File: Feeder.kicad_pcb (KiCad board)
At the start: 6 copper layers, 32 x 40 mm, 51 parts, among them T502 CMB1670V, U702 TPS562202, U710 TPS562202

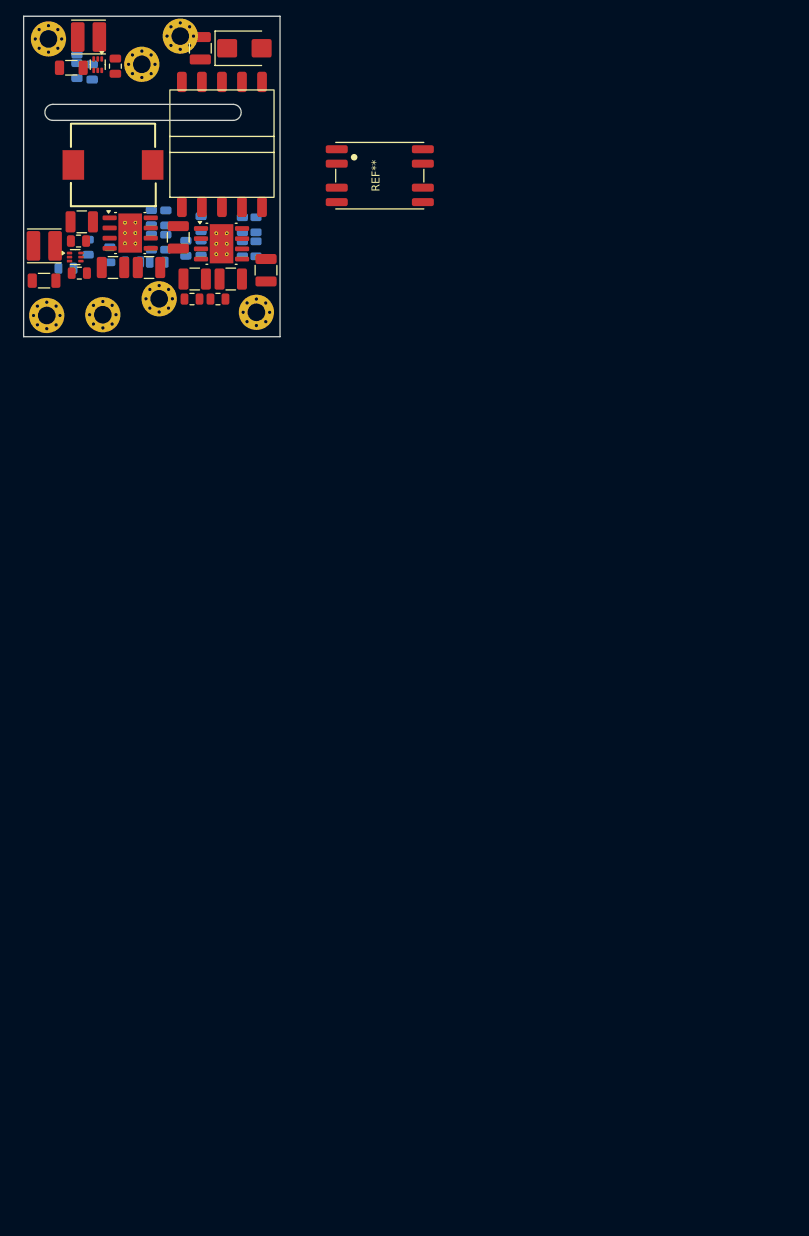
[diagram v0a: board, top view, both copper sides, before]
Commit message: Adding the placeholder for the capacitor board.
Signed-off-by: Jean Alinei <jean.alinei@owntech.org>
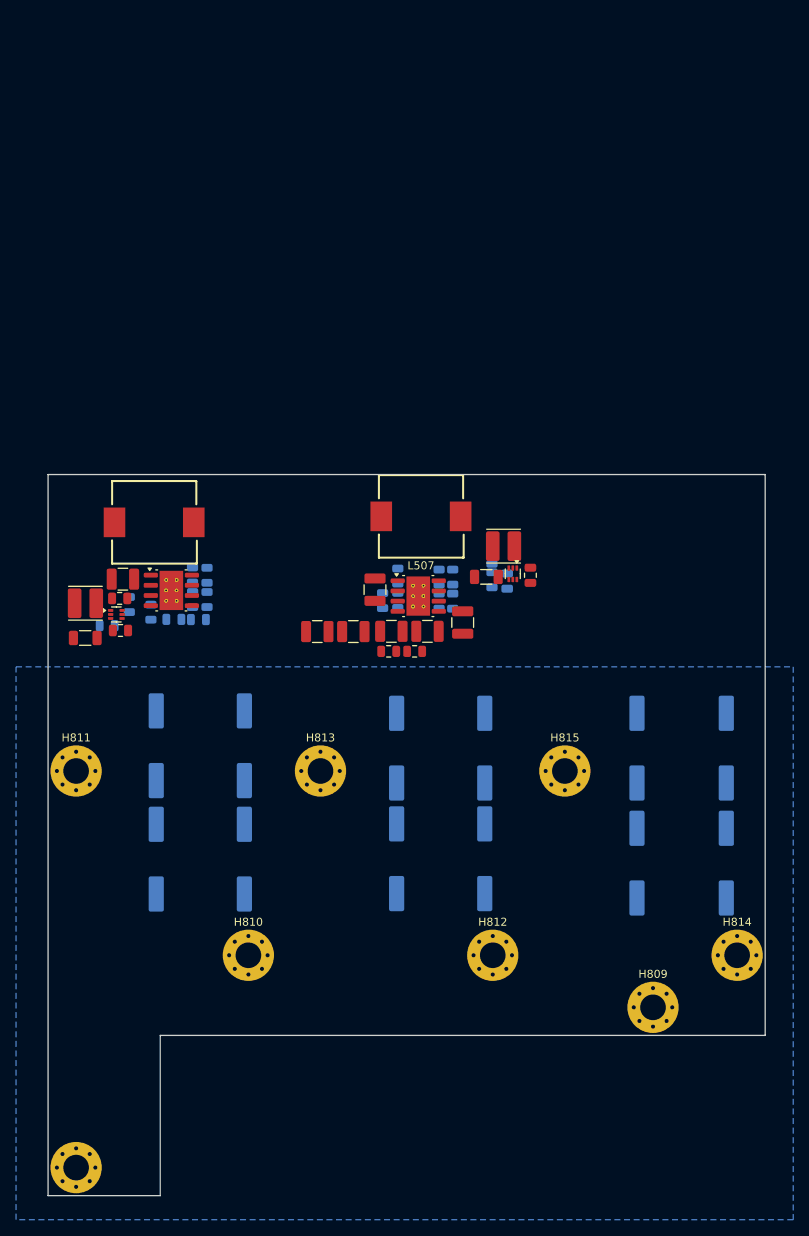
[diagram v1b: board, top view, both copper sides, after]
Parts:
- removed C527: 10uF, Footprints:C_1210_3225Metric
- removed D508: STTH4R02U, Diode_SMD:D_SMB
- removed H801, H802, H803, H804, H805, H806, H807: MountingHole_Pad, MountingHole:MountingHole_2.2mm_M2_Pad_Via
- removed REF**: VPT87BB-01B, Footprints:VPT87BB-01B
- removed T502: CMB1670V, Footprints:PA2467NL
- added C801: C_Polarized_US, Capacitor_SMD:CP_Elec_10x12.6, B.Cu at (69.5, 126.7)
- added C802: C_Polarized_US, Capacitor_SMD:CP_Elec_10x12.6, B.Cu at (58.5, 126.7)
- added C803: C_Polarized_US, Capacitor_SMD:CP_Elec_10x12.6, B.Cu at (88.5, 126.7)
- added C804: C_Polarized_US, Capacitor_SMD:CP_Elec_10x12.6, B.Cu at (99.5, 126.7)
- added C805: C_Polarized_US, Capacitor_SMD:CP_Elec_10x12.6, B.Cu at (129.7, 127.2)
- added C806: C_Polarized_US, Capacitor_SMD:CP_Elec_10x12.6, B.Cu at (118.5, 127.2)
- added C807: C_Polarized_US, Capacitor_SMD:CP_Elec_10x12.6, B.Cu at (69.5, 112.5)
- added C808: C_Polarized_US, Capacitor_SMD:CP_Elec_10x12.6, B.Cu at (58.5, 112.5)
- added C809: C_Polarized_US, Capacitor_SMD:CP_Elec_10x12.6, B.Cu at (88.5, 112.8)
- added C810: C_Polarized_US, Capacitor_SMD:CP_Elec_10x12.6, B.Cu at (99.5, 112.8)
- added C811: C_Polarized_US, Capacitor_SMD:CP_Elec_10x12.6, B.Cu at (129.7, 112.8)
- added C812: C_Polarized_US, Capacitor_SMD:CP_Elec_10x12.6, B.Cu at (118.5, 112.8)
- added H808: MountingHole_Pad, MountingHole:MountingHole_3.2mm_M3_Pad_Via, F.Cu at (48.5, 165.2)
- added H809: MountingHole_Pad, MountingHole:MountingHole_3.2mm_M3_Pad_Via, F.Cu at (120.5, 145.2)
- added H810: MountingHole_Pad, MountingHole:MountingHole_3.2mm_M3_Pad_Via, F.Cu at (70.0, 138.7)
- added H811: MountingHole_Pad, MountingHole:MountingHole_3.2mm_M3_Pad_Via, F.Cu at (48.5, 115.7)
- added H812: MountingHole_Pad, MountingHole:MountingHole_3.2mm_M3_Pad_Via, F.Cu at (100.5, 138.7)
- added H813: MountingHole_Pad, MountingHole:MountingHole_3.2mm_M3_Pad_Via, F.Cu at (79.0, 115.7)
- added H814: MountingHole_Pad, MountingHole:MountingHole_3.2mm_M3_Pad_Via, F.Cu at (131.0, 138.7)
- added H815: MountingHole_Pad, MountingHole:MountingHole_3.2mm_M3_Pad_Via, F.Cu at (109.5, 115.7)
- added L507: 220uH, Footprints:L-SMD_L10.5-W10.3_SLD10D50, F.Cu at (91.5, 83.9)
- moved C743 82.0 mm to (105.2, 91.3)
- moved R716 82.0 mm to (100.4, 88.9)
- moved R717 82.0 mm to (100.4, 91.8)
- moved C745 82.0 mm to (99.7, 91.5)
- moved L702 82.0 mm to (101.8, 87.6)
- moved U702 82.0 mm to (103.0, 91.1)
- moved C744 82.0 mm to (102.3, 92.0)
- moved C537 52.1 mm to (78.6, 98.3)
- moved C538 52.1 mm to (83.1, 98.3)
- moved R520 50.4 mm to (88.7, 91.4)
- moved C534 50.4 mm to (87.5, 100.8)
- moved R505 50.4 mm to (86.8, 94.4)
- moved R521 50.4 mm to (88.7, 94.4)
- moved U801 50.4 mm to (91.2, 93.9)
- moved C530 50.4 mm to (93.8, 94.5)
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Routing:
- added copper zone on B.Cu, net PGND
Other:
- board size 32 x 40 mm -> 89.5 x 90 mm

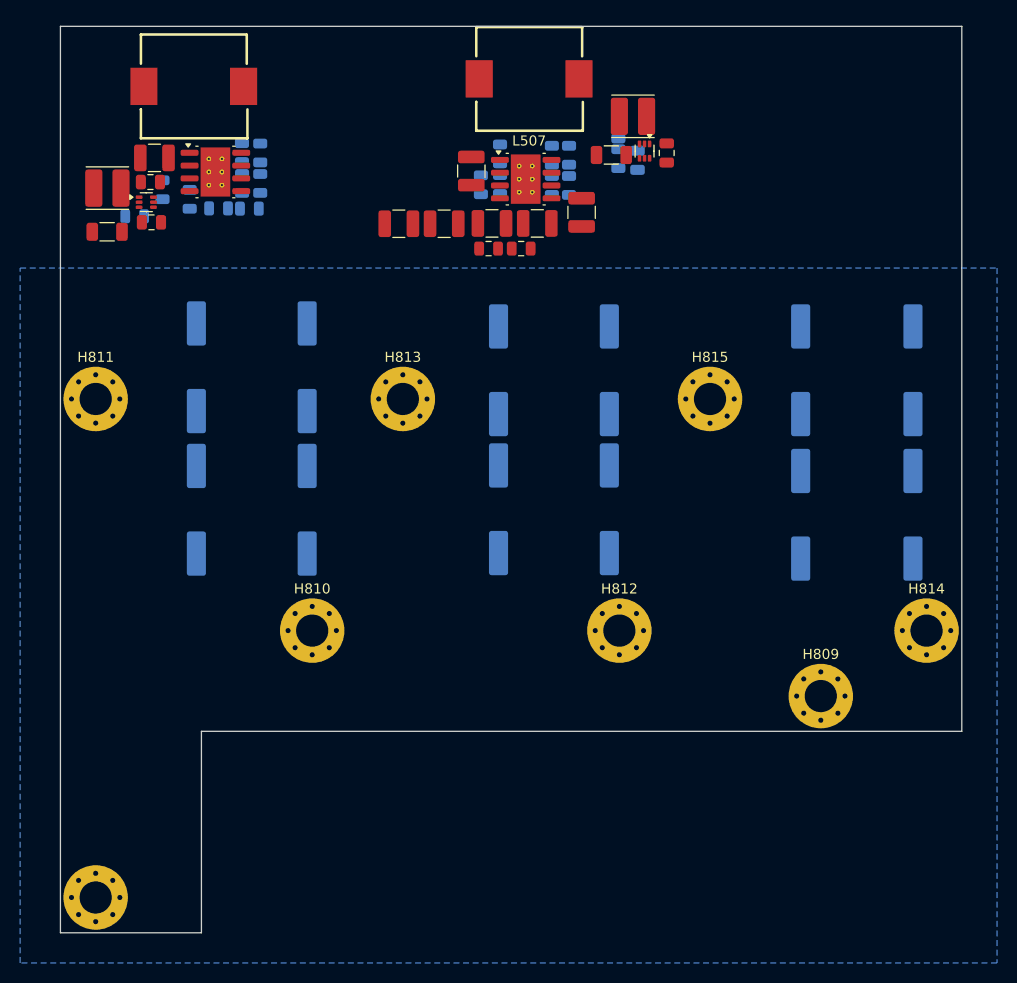
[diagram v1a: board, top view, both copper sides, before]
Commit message: v0 of the capacitor and feeder board
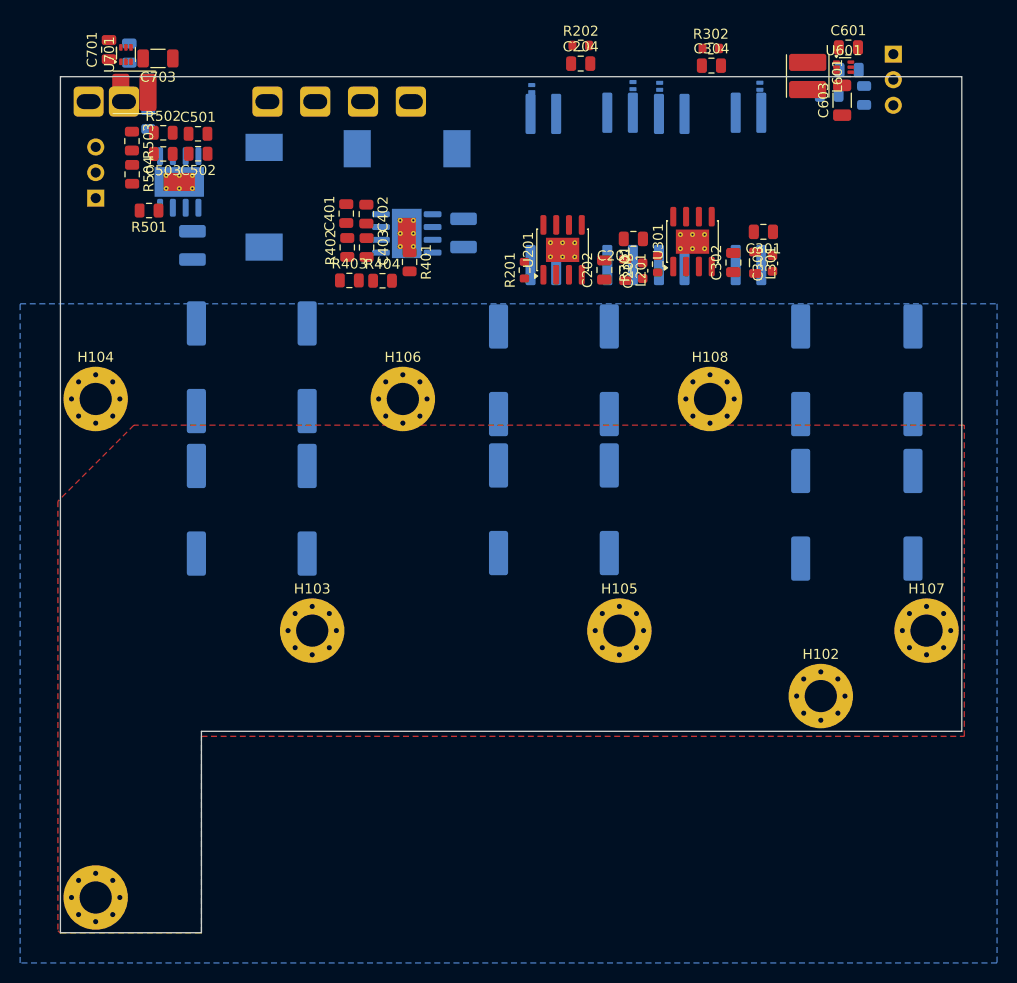
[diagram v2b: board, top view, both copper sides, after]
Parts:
- removed C529, C549: 10uF, Footprints:C_1210_3225Metric
- removed C530, C531, C532, C545, C546, C547: 1uF, Footprints:C_0805_2012Metric
- removed C533, C534: 470nF, Footprints:C_0805_2012Metric
- removed C535, C536, C537, C538: 4.7uF, Footprints:C_1210_3225Metric
- removed C743, C746: 10uF, Capacitor_SMD:C_0805_2012Metric
- removed C744, C747: 100nF, Capacitor_SMD:C_0805_2012Metric
- removed C745, C748: 47uF, Capacitor_SMD:C_1206_3216Metric
- removed L504: 10uH, Inductor_SMD:L_1210_3225Metric
- removed L506, L507: 220uH, Footprints:L-SMD_L10.5-W10.3_SLD10D50
- removed L702, L709: 4.7uH - 80mR, Inductor_SMD:L_Cenker_CKCS4020
- removed R505, R524: 100k, Footprints:R_0805_2012Metric
- removed R520, R523, R525, R526: 10R, Footprints:R_0805_2012Metric
- removed R521, R527: 38.3k, Footprints:R_0805_2012Metric
- removed R716, R718: 56k, Footprints:R_0805_2012Metric
- removed R717, R719: 10k, Footprints:R_0805_2012Metric
- removed U702, U710: TPS562202, Package_TO_SOT_SMD:SOT-563
- removed U801, U802: ~, Package_SO:Texas_R-PDSO-G8_EP2.95x4.9mm_Mask2.4x3.1mm_ThermalVias
- added C201: 10uF, Capacitor_SMD:C_0805_2012Metric, F.Cu at (101.9, 99.8)
- added C202: 10uF, Capacitor_SMD:C_0805_2012Metric, F.Cu at (99.0, 102.9)
- added C203: 100nF, Capacitor_SMD:C_0603_1608Metric, F.Cu at (102.8, 103.0)
- added C204: 10uF, Capacitor_SMD:C_0805_2012Metric, F.Cu at (96.7, 82.4)
- added C301: 10uF, Capacitor_SMD:C_0805_2012Metric, F.Cu at (114.8, 99.1)
- added C302: 10uF, Capacitor_SMD:C_0805_2012Metric, F.Cu at (111.8, 102.2)
- added C303: 100nF, Capacitor_SMD:C_0603_1608Metric, F.Cu at (115.7, 102.2)
- added C304: 10uF, Capacitor_SMD:C_0805_2012Metric, F.Cu at (109.6, 82.6)
- added C401: 1uF, Footprints:C_0805_2012Metric, F.Cu at (73.4, 97.3)
- added C402: 1uF, Footprints:C_0805_2012Metric, F.Cu at (75.4, 97.3)
- added C403: 1uF, Footprints:C_0805_2012Metric, F.Cu at (75.4, 100.7)
- added C404: 10uF, Footprints:C_1210_3225Metric, B.Cu at (85.0, 99.2)
- added C501: 1uF, Footprints:C_0805_2012Metric, F.Cu at (58.7, 89.4)
- added C502: 1uF, Footprints:C_0805_2012Metric, F.Cu at (58.7, 91.3)
- added C503: 1uF, Footprints:C_0805_2012Metric, F.Cu at (55.2, 91.4)
- added C504: 10uF, Footprints:C_1210_3225Metric, B.Cu at (58.1, 100.5)
- added C601: 10uF, Capacitor_SMD:C_0805_2012Metric, F.Cu at (123.2, 80.8)
- added C602: 100nF, Capacitor_SMD:C_0805_2012Metric, B.Cu at (123.3, 83.0)
- added C603: 47uF, Capacitor_SMD:C_1206_3216Metric, F.Cu at (122.6, 86.0)
- added C701: 10uF, Capacitor_SMD:C_0805_2012Metric, F.Cu at (49.8, 81.0)
- added C702: 100nF, Capacitor_SMD:C_0805_2012Metric, B.Cu at (51.8, 81.4)
- added C703: 47uF, Capacitor_SMD:C_1206_3216Metric, F.Cu at (54.7, 81.9)
- added D201: PMEG4010, Diode_SMD:D_SOD-882, B.Cu at (101.8, 84.6)
- added D202: PMEG4010, Diode_SMD:D_SOD-882, B.Cu at (91.8, 84.9)
- added D301: PMEG4010, Diode_SMD:D_SOD-882, B.Cu at (114.5, 84.7)
- added D302: PMEG4010, Diode_SMD:D_SOD-882, B.Cu at (104.5, 84.7)
- added J101: Conn_01x03_Pin, Connector_PinHeader_2.54mm:PinHeader_1x03_P2.54mm_Vertical, B.Cu at (127.7, 81.5)
- added J102: Conn_01x03_Pin, Connector_PinHeader_2.54mm:PinHeader_1x03_P2.54mm_Vertical, B.Cu at (48.5, 95.8)
- added L201: 10uH, Inductor_SMD:L_0805_2012Metric, F.Cu at (101.1, 102.9)
- added L301: 10uH, Inductor_SMD:L_0805_2012Metric, F.Cu at (114.0, 102.2)
- added L401: 220uH, Footprints:L-SMD_L10.5-W10.3_SLD10D50, B.Cu at (79.4, 90.9)
- added L501: 220uH, Footprints:L-SMD_L10.5-W10.3_SLD10D50, B.Cu at (65.2, 95.7)
- added L601: 4.7uH - 80mR, Inductor_SMD:L_Cenker_CKCS4020, F.Cu at (119.2, 83.6)
- added L701: 4.7uH - 80mR, Inductor_SMD:L_Cenker_CKCS4020, F.Cu at (52.3, 85.3)
- added R201: R_Small, Resistor_SMD:R_0603_1608Metric, F.Cu at (91.1, 102.9)
- added R202: 4.7k, Resistor_SMD:R_0603_1608Metric, F.Cu at (96.7, 80.6)
- added R301: R_Small, Resistor_SMD:R_0603_1608Metric, F.Cu at (104.3, 102.3)
- added R302: 4.7k, Resistor_SMD:R_0603_1608Metric, F.Cu at (109.6, 80.9)
- added R401: 100k, Footprints:R_0805_2012Metric, F.Cu at (79.7, 102.1)
- added R402: 10R, Footprints:R_0805_2012Metric, F.Cu at (73.5, 100.7)
- added R403: 10R, Footprints:R_0805_2012Metric, F.Cu at (73.7, 103.9)
- added R404: 38.3k, Footprints:R_0805_2012Metric, F.Cu at (77.0, 104.0)
- added R501: 100k, Footprints:R_0805_2012Metric, F.Cu at (53.8, 97.0)
- added R502: 10R, Footprints:R_0805_2012Metric, F.Cu at (55.2, 89.3)
- added R503: 10R, Footprints:R_0805_2012Metric, F.Cu at (52.1, 90.1)
- added R504: 38.3k, Footprints:R_0805_2012Metric, F.Cu at (52.1, 93.4)
- added R601: 56k, Footprints:R_0805_2012Metric, B.Cu at (121.3, 85.5)
- added R602: 10k, Footprints:R_0805_2012Metric, B.Cu at (124.8, 85.6)
- added R701: 56k, Footprints:R_0805_2012Metric, B.Cu at (53.7, 84.8)
- added R702: 10k, Footprints:R_0805_2012Metric, B.Cu at (53.7, 88.0)
- added REF**: LS05-26BxxR2_RA, feeder:LS05-26BxxR2_RA, B.Cu at (79.8, 86.2)
- added TR201: CMT88F0U, feeder:CMT88F0U, B.Cu at (96.8, 94.9)
- added TR301: CMT88F0U, feeder:CMT88F0U, B.Cu at (109.5, 94.9)
- added U201: CMP6793RE, Package_SO:SOIC-8-1EP_3.9x4.9mm_P1.27mm_EP2.41x3.3mm_ThermalVias, F.Cu at (94.9, 100.9)
- added U301: CMP6793RE, Package_SO:SOIC-8-1EP_3.9x4.9mm_P1.27mm_EP2.41x3.3mm_ThermalVias, F.Cu at (107.8, 100.1)
- added U401: ~, Package_SO:Texas_R-PDSO-G8_EP2.95x4.9mm_Mask2.4x3.1mm_ThermalVias, B.Cu at (79.4, 99.3)
- added U501: ~, Package_SO:Texas_R-PDSO-G8_EP2.95x4.9mm_Mask2.4x3.1mm_ThermalVias, B.Cu at (56.8, 94.2)
- added U601: TPS562202, Package_TO_SOT_SMD:SOT-563, F.Cu at (122.8, 82.8)
- added U701: TPS562202, Package_TO_SOT_SMD:SOT-563, F.Cu at (51.5, 81.5)
- turned C107 to -90 degrees
- turned C109 to -90 degrees
- turned C111 to -90 degrees
- turned C113 to -90 degrees
- turned C115 to -90 degrees
- turned C117 to -90 degrees
- renumbered C801 to C107, C807 to C108, C802 to C109, C808 to C110, C803 to C111, C809 to C112, C804 to C113, C810 to C114, C805 to C115, C811 to C116, C806 to C117, C812 to C118, H808 to H101, H809 to H102, H810 to H103, H811 to H104, H812 to H105, H813 to H106, H814 to H107, H815 to H108
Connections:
- C107 pad 2: Net-(C801-Pad2) -> PGND
- C108 pad 1: Net-(C801-Pad2) -> /VHigh
- C109 pad 2: Net-(C802-Pad2) -> PGND
- C110 pad 1: Net-(C802-Pad2) -> /VHigh
- C111 pad 2: Net-(C803-Pad2) -> PGND
- C112 pad 1: Net-(C803-Pad2) -> /VHigh
- C113 pad 2: Net-(C804-Pad2) -> PGND
- C114 pad 1: Net-(C804-Pad2) -> /VHigh
- C115 pad 2: Net-(C805-Pad2) -> PGND
- C116 pad 1: Net-(C805-Pad2) -> /VHigh
- C117 pad 2: Net-(C806-Pad2) -> PGND
- C118 pad 1: Net-(C806-Pad2) -> /VHigh
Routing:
- added copper zone on F.Cu, net /VHigh
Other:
- board size 89.5 x 90 mm -> 89.5 x 85 mm
- copper layers 6 -> 4

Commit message: added eeprom and isolation slots
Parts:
- removed REF**: LS05-26BxxR2_RA, feeder:LS05-26BxxR2_RA
- added C101: 470nF, Footprints:C_0805_2012Metric, F.Cu at (-45.0, -107.0)
- added C102: 470nF, Footprints:C_0805_2012Metric, F.Cu at (-45.0, -104.3)
- added C103: 4.7uF, Footprints:C_1210_3225Metric, F.Cu at (-49.7, -110.6)
- added C104: 4.7uF, Footprints:C_1210_3225Metric, F.Cu at (-49.7, -106.7)
- added C105: 4.7uF, Footprints:C_1210_3225Metric, F.Cu at (-49.7, -102.9)
- added C106: 4.7uF, Footprints:C_1210_3225Metric, F.Cu at (-49.7, -99.0)
- added C119: 100nF, Capacitor_SMD:C_0603_1608Metric, F.Cu at (84.2, -83.5)
- added J103: Conn_01x02_Pin, Connector_PinHeader_2.54mm:PinHeader_1x02_P2.54mm_Vertical, F.Cu at (82.6, -91.8)
- added L101: 10uH, Inductor_SMD:L_1210_3225Metric, F.Cu at (-44.2, -110.4)
- added R101: 10k, Capacitor_SMD:C_0603_1608Metric, F.Cu at (87.1, -86.0)
- added U101: XBLW 24C02S(XBLW), Package_TO_SOT_SMD:SOT-23-5, F.Cu at (84.2, -86.0)
- C204, C304, R202, R302: moved to B.Cu
- J101: value Conn_01x03_Pin -> Conn_02x03_Odd_Even; footprint Connector_PinHeader_2.54mm:PinHeader_1x03_P2.54mm_Vertical -> Connector_PinHeader_2.54mm:PinHeader_2x03_P2.54mm_Vertical
- moved D202 183.2 mm to (52.7, -94.0)
- moved C107 183.1 mm to (29.5, -52.0)
- moved C108 183.1 mm to (29.5, -66.2)
- moved C109 183.1 mm to (18.5, -52.0)
- moved C110 183.1 mm to (18.5, -66.2)
- moved H101 183.1 mm to (8.75, -13.5)
- moved H102 183.1 mm to (80.8, -33.5)
- moved H103 183.1 mm to (30.2, -40.0)
- moved H104 183.1 mm to (8.75, -63.0)
- moved H105 183.1 mm to (60.8, -40.0)
- moved H106 183.1 mm to (39.2, -63.0)
- moved H107 183.1 mm to (91.2, -40.0)
- moved H108 183.1 mm to (69.8, -63.0)
- moved C115 183.0 mm to (90.0, -51.5)
- moved C116 183.0 mm to (90.0, -65.8)
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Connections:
- net /dc-dc_12-5/VIN renamed +12V_DGND
- net /dc-dc_12-5/VOUT renamed +5V_DGND
- C204 pad 2: /dc-dc_12-5/IN_GND -> DGND
- C304 pad 2: /dc-dc_12-5/IN_GND -> DGND
- C601 pad 2: /dc-dc_12-5/IN_GND -> DGND
- C603 pad 2: /dc-dc_12-5/IN_GND -> DGND
- J101 pad 3: /dc-dc_12-5/IN_GND -> DGND
- R202 pad 2: /dc-dc_12-5/IN_GND -> DGND
- R302 pad 2: /dc-dc_12-5/IN_GND -> DGND
- R602 pad 2: /dc-dc_12-5/IN_GND -> DGND
- TR201 pad 6: /dc-dc_12-5/IN_GND -> DGND
- TR201 pad 7: /dc-dc_12-5/IN_GND -> DGND
- TR301 pad 6: /dc-dc_12-5/IN_GND -> DGND
- TR301 pad 7: /dc-dc_12-5/IN_GND -> DGND
- U601 pad 3: /dc-dc_12-5/IN_GND -> DGND
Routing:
- net +12V_DGND: track 0.00 -> 61.8 mm, vias 0 -> 1
- net +5V_DGND: track 0.00 -> 18.2 mm, vias 0 -> 2
- net Net-(J101-Pin_6): track 0.00 -> 15.2 mm
- net Net-(J101-Pin_5): track 0.00 -> 14.0 mm
- net DGND: track 0.00 -> 9.14 mm, vias 0 -> 9
- net Net-(J103-Pin_1): track 0.00 -> 8.27 mm
- net Net-(U601-SW): track 0.00 -> 5.84 mm, vias 0 -> 1
- net Net-(U601-VBST): track 0.00 -> 3.49 mm, vias 0 -> 1
- net Net-(U601-VFB): track 0.00 -> 2.53 mm
- net Net-(D302-A): track 0.00 -> 2.52 mm
- net Net-(D202-A): track 0.00 -> 2.51 mm
- net Net-(D301-A): track 0.00 -> 2.40 mm
- net Net-(D201-A): track 0.00 -> 2.40 mm
- added copper zone on B.Cu, net DGND
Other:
- board size 89.5 x 85 mm -> 91 x 85 mm
